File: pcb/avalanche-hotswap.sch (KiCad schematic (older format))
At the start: 141 parts, among them J1 TRRS, J3 OLED, P1 i2c_pin, P2 i2c_pin, SW0 SW_Push, SW1 SW_Push, SW10 SW_Push, SW11 SW_Push, SW12 SW_Push, SW13 SW_Push, SW14 SW_Push, SW15 SW_Push, SW16 SW_Push, SW17 SW_Push, SW18 SW_Push, SW19 SW_Push, SW2 SW_Push, SW20 SW_Push, SW21 SW_Push, SW22 SW_Push, SW23 SW_Push, SW24 SW_Push, SW25 SW_Push, SW26 SW_Push, SW27 SW_Push, SW28 SW_Push, SW29 SW_Push, SW3 SW_Push, SW30 SW_Push, SW31 SW_Push, SW32 SW_Push, SW4 SW_Push, SW5 SW_Push, SW6 SW_Push, SW7 SW_Push, SW8 SW_Push, SW9 SW_Push, U1 ProMicro

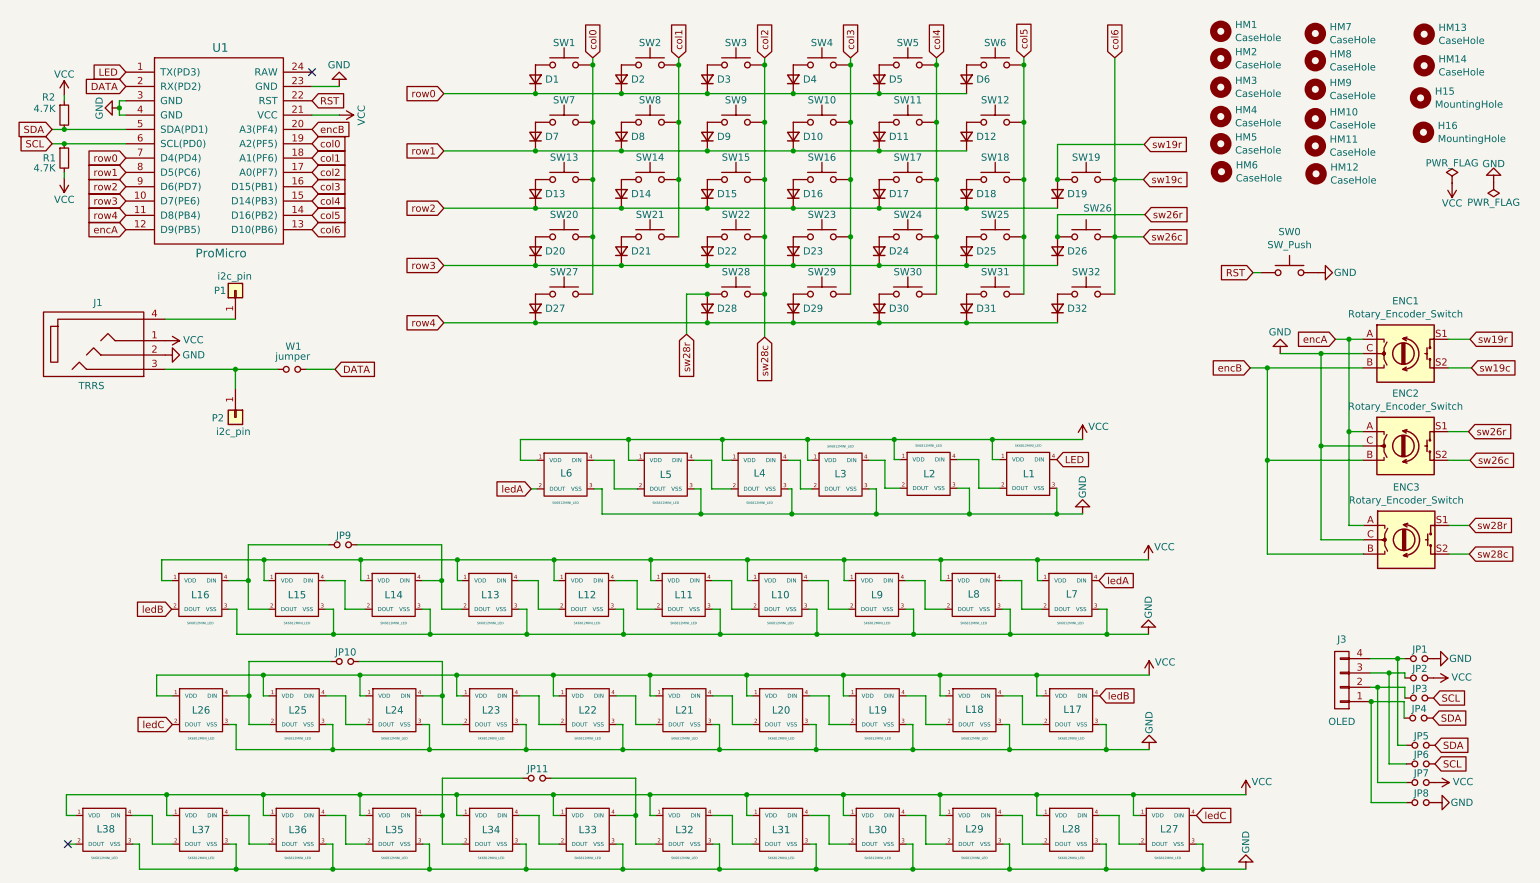
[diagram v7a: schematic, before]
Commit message: Removed SW19 (and related)
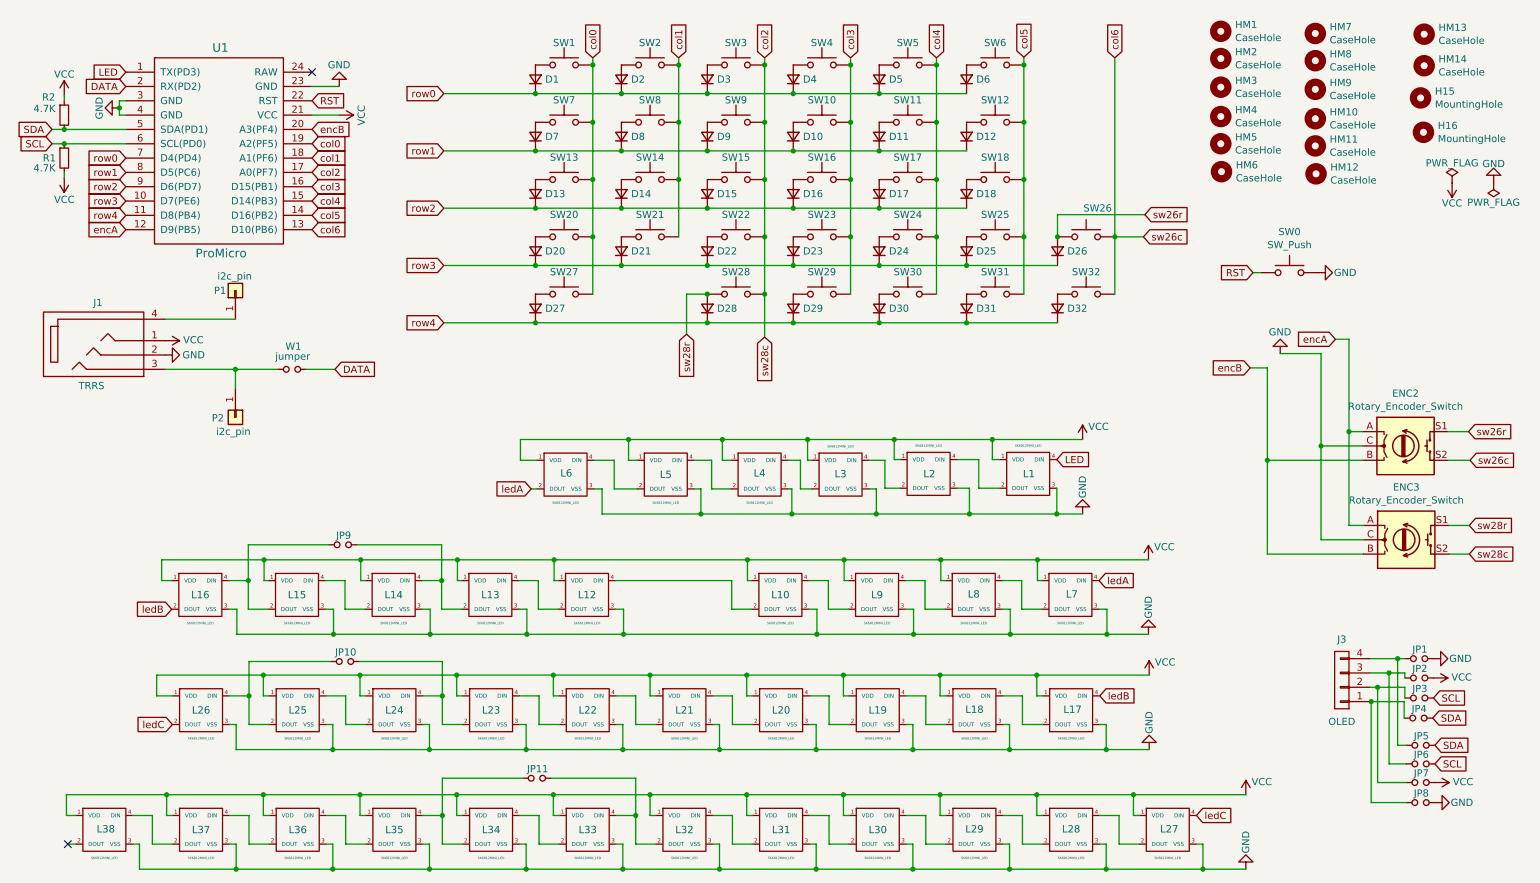
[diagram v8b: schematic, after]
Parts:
- removed D19: 1N4148, used_footprints:diode_TH_SMD, symbol Device:D_Small
- removed ENC1: Rotary_Encoder_Switch, used_footprints:RotaryEncoder_Alps_EC11E-Switch_Vertical_H20mm-keebio_modified, symbol Device:Rotary_Encoder_Switch
- removed L11: SK6812MINI_LED, used_footprints:YS-SK6812MINI-E, symbol avalanche-hotswap:SK6812MINI_LED
- removed SW19: SW_Push, used_footprints:CherryMX_MidHeight_Hotswap_1u, symbol Switch:SW_Push
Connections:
- net at L10.2 (DOUT): now also L12.4 (DIN)
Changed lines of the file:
@@
 	0    -1   -1   0
 $EndComp
-$Comp
-L Switch:SW_Push SW19
-U 1 1 605336C7
-P 7990 1690
-F 0 "SW19" H 7990 1845 50  0000 C CNN
-F 1 "SW_Push" H 7990 1884 50  0001 C CNN
-F 2 "used_footprints:CherryMX_MidHeight_Hotswap_1u" H 7990 1890 50  0001 C CNN
-F 3 "~" H 7990 1890 50  0001 C CNN
-	1    7990 1690
-	1    0    0    -1
-$EndComp
-$Comp
-L Device:D_Small D19
-U 1 1 605336CD
-P 7790 1790
-F 0 "D19" V 7790 1722 50  0000 R CNN
-F 1 "1N4148" V 7745 1722 50  0001 R CNN
-F 2 "used_footprints:diode_TH_SMD" V 7790 1790 50  0001 C CNN
-F 3 "~" V 7790 1790 50  0001 C CNN
-	1    7790 1790
-	0    -1   -1   0
-$EndComp
-Wire Wire Line
-	8190 840  8190 1690
 Wire Wire Line
 	6545 1090 7155 1090
@@
 	7555 1290 7555 1690
 Connection ~ 7555 1290
-Wire Wire Line
-	7155 1890 7790 1890
-Connection ~ 7155 1890
 Wire Wire Line
 	3505 2290 4145 2290
@@
 $EndComp
 Wire Wire Line
-	8190 1690 8190 2090
-Connection ~ 8190 1690
-Wire Wire Line
 	7155 2290 7790 2290
 Connection ~ 7155 2290
@@
 	1560 2665 2050 2665
 $Comp
-L Device:Rotary_Encoder_Switch ENC1
-U 1 1 6071F2CB
-P 10220 2905
-F 0 "ENC1" H 10220 3272 50  0000 C CNN
-F 1 "Rotary_Encoder_Switch" H 10220 3181 50  0000 C CNN
-F 2 "used_footprints:RotaryEncoder_Alps_EC11E-Switch_Vertical_H20mm-keebio_modified" H 10070 3065 50  0001 C CNN
-F 3 "~" H 10220 3165 50  0001 C CNN
-	1    10220 2905
-	1    0    0    -1
-$EndComp
-$Comp
 L Device:Rotary_Encoder_Switch ENC2
 U 1 1 607429F7
@@
 encA
 Wire Wire Line
-	9920 2805 9825 2805
-Wire Wire Line
 	9920 3450 9825 3450
 Wire Wire Line
 	9825 3450 9825 2805
-Connection ~ 9825 2805
 Wire Wire Line
 	9825 2805 9730 2805
@@
 Wire Wire Line
 	9255 3650 9255 3005
-Connection ~ 9255 3005
 Wire Wire Line
 	9255 3005 9135 3005
@@
 $EndComp
 Wire Wire Line
-	9920 2905 9630 2905
-Wire Wire Line
 	9920 3550 9630 3550
 Wire Wire Line
 	9630 3550 9630 2905
-Connection ~ 9630 2905
 Wire Wire Line
 	9630 2905 9345 2905
@@
 Connection ~ 9630 3550
 Wire Wire Line
-	9255 3005 9920 3005
-Wire Wire Line
 	9255 3650 9920 3650
 Wire Wire Line
@@
 	4545 2090 4545 2490
 Connection ~ 4545 2090
-Text GLabel 8395 1445 2    50   Input ~ 0
-sw19r
-Text GLabel 8390 1690 2    50   Input ~ 0
-sw19c
-Wire Wire Line
-	8190 1690 8390 1690
 Text GLabel 8390 2090 2    50   Input ~ 0
 sw26c
@@
 Text GLabel 10660 3450 2    50   Input ~ 0
 sw26r
-Text GLabel 10670 2805 2    50   Input ~ 0
-sw19r
-Text GLabel 10680 3005 2    50   Input ~ 0
-sw19c
-Wire Wire Line
-	10520 2805 10670 2805
-Wire Wire Line
-	10520 3005 10680 3005
 Wire Wire Line
 	10520 3450 10660 3450
@@
 Connection ~ 7790 2090
 Wire Wire Line
-	7790 1690 7790 1445
-Wire Wire Line
-	7790 1445 8395 1445
-Connection ~ 7790 1690
-Wire Wire Line
 	3505 1890 4145 1890
 Wire Wire Line
@@
 $EndComp
 $Comp
-L avalanche-hotswap:SK6812MINI_LED L11
-U 1 1 612DAE1D
-P 5180 4590
-F 0 "L11" H 5180 4590 51  0000 C CNN
-F 1 "SK6812MINI_LED" H 5180 4393 16  0000 C CNN
-F 2 "used_footprints:YS-SK6812MINI-E" H 5180 4590 60  0001 C CNN
-F 3 "" H 5180 4590 60  0001 C CNN
-	1    5180 4590
-	1    0    0    -1
-$EndComp
-$Comp
 L avalanche-hotswap:SK6812MINI_LED L12
 U 1 1 612E9A39
@@
 	6110 4865 6785 4865
 Wire Wire Line
-	5380 4690 5435 4690
-Wire Wire Line
-	5435 4690 5435 4865
-Connection ~ 5435 4865
-Wire Wire Line
-	5435 4865 6110 4865
-Wire Wire Line
 	4705 4690 4760 4690
 Wire Wire Line
@@
 Connection ~ 4760 4865
 Wire Wire Line
-	4760 4865 5435 4865
-Wire Wire Line
 	4030 4690 4085 4690
 Wire Wire Line
@@
 	5625 4345 6300 4345
 Wire Wire Line
-	4980 4490 4950 4490
-Wire Wire Line
-	4950 4490 4950 4345
-Connection ~ 4950 4345
-Wire Wire Line
-	4950 4345 5625 4345
-Wire Wire Line
 	4305 4490 4275 4490
 Wire Wire Line
@@
 Connection ~ 4275 4345
 Wire Wire Line
-	4275 4345 4950 4345
-Wire Wire Line
 	3630 4490 3600 4490
 Wire Wire Line
@@
 Wire Wire Line
 	5515 4690 5515 4490
-Wire Wire Line
-	5515 4490 5380 4490
 Wire Wire Line
 	4305 4690 4165 4690
@@
 	870  5985 870  6130
 Connection ~ 1570 5985
-Wire Wire Line
-	4980 4690 4855 4690
-Wire Wire Line
-	4855 4690 4855 4490
-Wire Wire Line
-	4855 4490 4705 4490
 Wire Wire Line
 	1500 5295 1610 5295
@@
 	1    0    0    -1
 $EndComp
+Wire Wire Line
+	8190 840  8190 2090
+Wire Wire Line
+	4275 4345 5625 4345
+Wire Wire Line
+	4760 4865 6110 4865
+Wire Wire Line
+	4705 4490 5515 4490
 $EndSCHEMATC
